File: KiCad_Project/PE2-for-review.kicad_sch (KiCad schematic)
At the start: 61 parts, among them J1 C2977719 miniUSBb, J2 Conn_01x06, J4 Conn_01x05, SW1 C455091, SW10 C2985742, SW11 C455091, SW12 SW_Push, SW13 SW_Push, SW14 SW_Push, SW15 C455091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

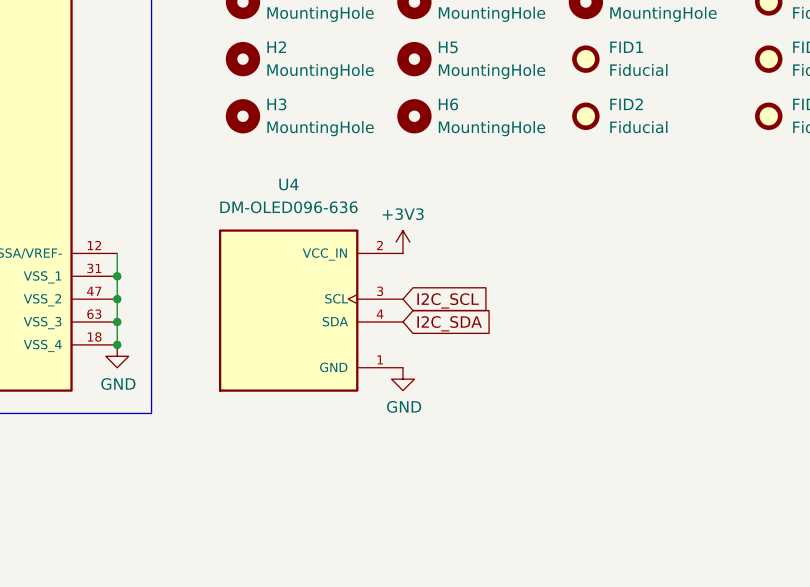
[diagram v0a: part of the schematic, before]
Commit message: prettified schematic slightly + added schematic pdf
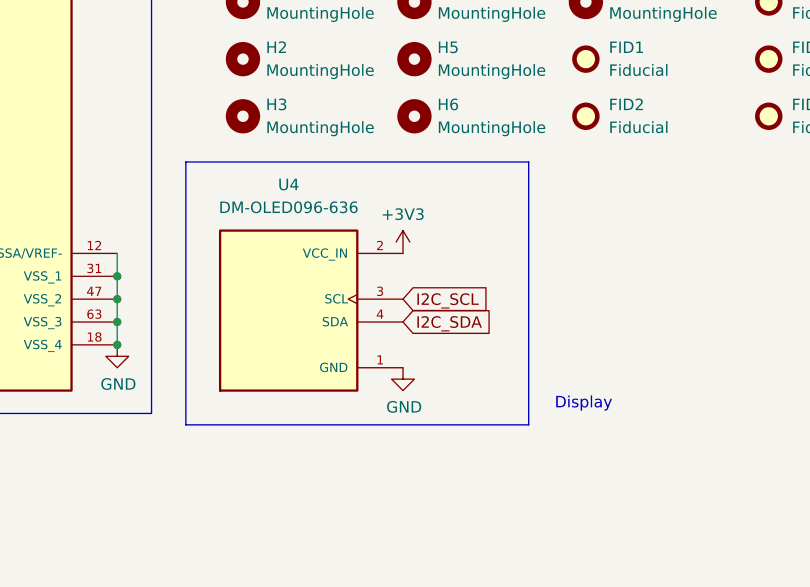
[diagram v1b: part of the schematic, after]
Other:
- note added: "Display"
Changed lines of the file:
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@@
+	)
+	(rectangle
+		(start 200.66 134.62)
+		(end 238.76 163.83)
+		(stroke
+			(width 0)
+			(type default)
+		)
+		(fill
+			(type none)
+		)
 	)
 	(rectangle
@@
 		(effects
 			(font
+				(size 1.27 1.27)
+			)
+		)
+	)
+	(text "Display\n"
+		(exclude_from_sim no)
+		(at 244.856 161.544 0)
+		(effects
+			(font
